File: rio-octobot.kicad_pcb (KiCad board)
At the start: 2 copper layers, 100 x 100 mm, 128 parts, among them J1 Conn_01x06, J10 Conn_01x03, J11 Conn_01x03, J12 Conn_01x03, J13 Conn_01x13, J14 Conn_01x12, J2 Conn_01x06, J3 Conn_01x06, J4 Conn_01x06, J5 Conn_01x06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

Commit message: fixing labels / add some values
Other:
- board text added: "12v GND 5v EN STP DIR"
- board text removed: "12v GND 5v EN DIR STP"
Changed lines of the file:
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@@
     (effects (font (size 1 1) (thickness 0.15)) (justify left bottom))
   )
-  (gr_text "12v GND 5v EN DIR STP" (at 127 74.93 90) (layer "F.SilkS")
+  (gr_text "12v GND 5v EN STP DIR" (at 127 74.93 90) (layer "F.SilkS")
     (effects (font (size 1 1) (thickness 0.15)) (justify left bottom))
   )
@@
     (effects (font (size 1 1) (thickness 0.15)) (justify left bottom))
   )
-  (gr_text "12v GND 5v EN DIR STP" (at 91.44 74.93 90) (layer "F.SilkS")
+  (gr_text "12v GND 5v EN STP DIR" (at 91.44 74.93 90) (layer "F.SilkS")
     (effects (font (size 1 1) (thickness 0.15)) (justify left bottom))
   )
@@
     (effects (font (size 1 1) (thickness 0.15)) (justify left bottom))
   )
-  (gr_text "12v GND 5v EN DIR STP" (at 73.66 74.93 90) (layer "F.SilkS")
+  (gr_text "12v GND 5v EN STP DIR" (at 73.66 74.93 90) (layer "F.SilkS")
     (effects (font (size 1 1) (thickness 0.15)) (justify left bottom))
   )
@@
     (effects (font (size 1 1) (thickness 0.15)) (justify left bottom))
   )
-  (gr_text "12v GND 5v EN DIR STP" (at 82.55 74.93 90) (layer "F.SilkS")
+  (gr_text "12v GND 5v EN STP DIR" (at 82.55 74.93 90) (layer "F.SilkS")
     (effects (font (size 1 1) (thickness 0.15)) (justify left bottom))
   )
@@
     (effects (font (size 1 1) (thickness 0.15)) (justify left bottom))
   )
-  (gr_text "12v GND 5v EN DIR STP" (at 109.22 74.93 90) (layer "F.SilkS")
+  (gr_text "12v GND 5v EN STP DIR" (at 109.22 74.93 90) (layer "F.SilkS")
     (effects (font (size 1 1) (thickness 0.15)) (justify left bottom))
   )
@@
     (effects (font (size 2 2) (thickness 0.15)) (justify left bottom))
   )
-  (gr_text "12v GND 5v EN DIR STP" (at 118.11 74.93 90) (layer "F.SilkS")
+  (gr_text "12v GND 5v EN STP DIR" (at 118.11 74.93 90) (layer "F.SilkS")
     (effects (font (size 1 1) (thickness 0.15)) (justify left bottom))
   )
@@
     (effects (font (size 1 1) (thickness 0.15)) (justify left bottom))
   )
-  (gr_text "12v GND 5v EN DIR STP" (at 100.33 74.93 90) (layer "F.SilkS")
+  (gr_text "12v GND 5v EN STP DIR" (at 100.33 74.93 90) (layer "F.SilkS")
     (effects (font (size 1 1) (thickness 0.15)) (justify left bottom))
   )

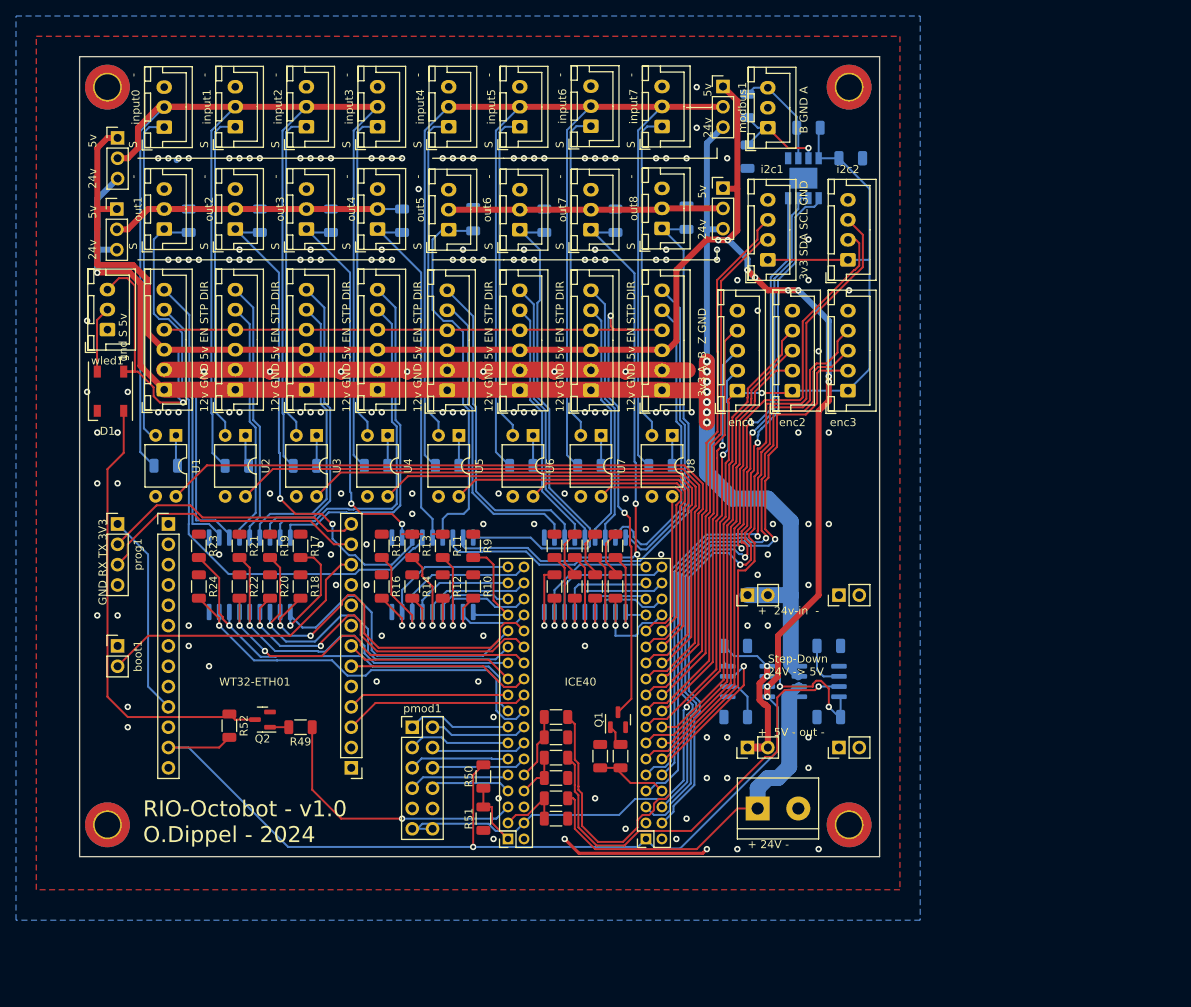
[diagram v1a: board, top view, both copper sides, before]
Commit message: removing level shifter from wled
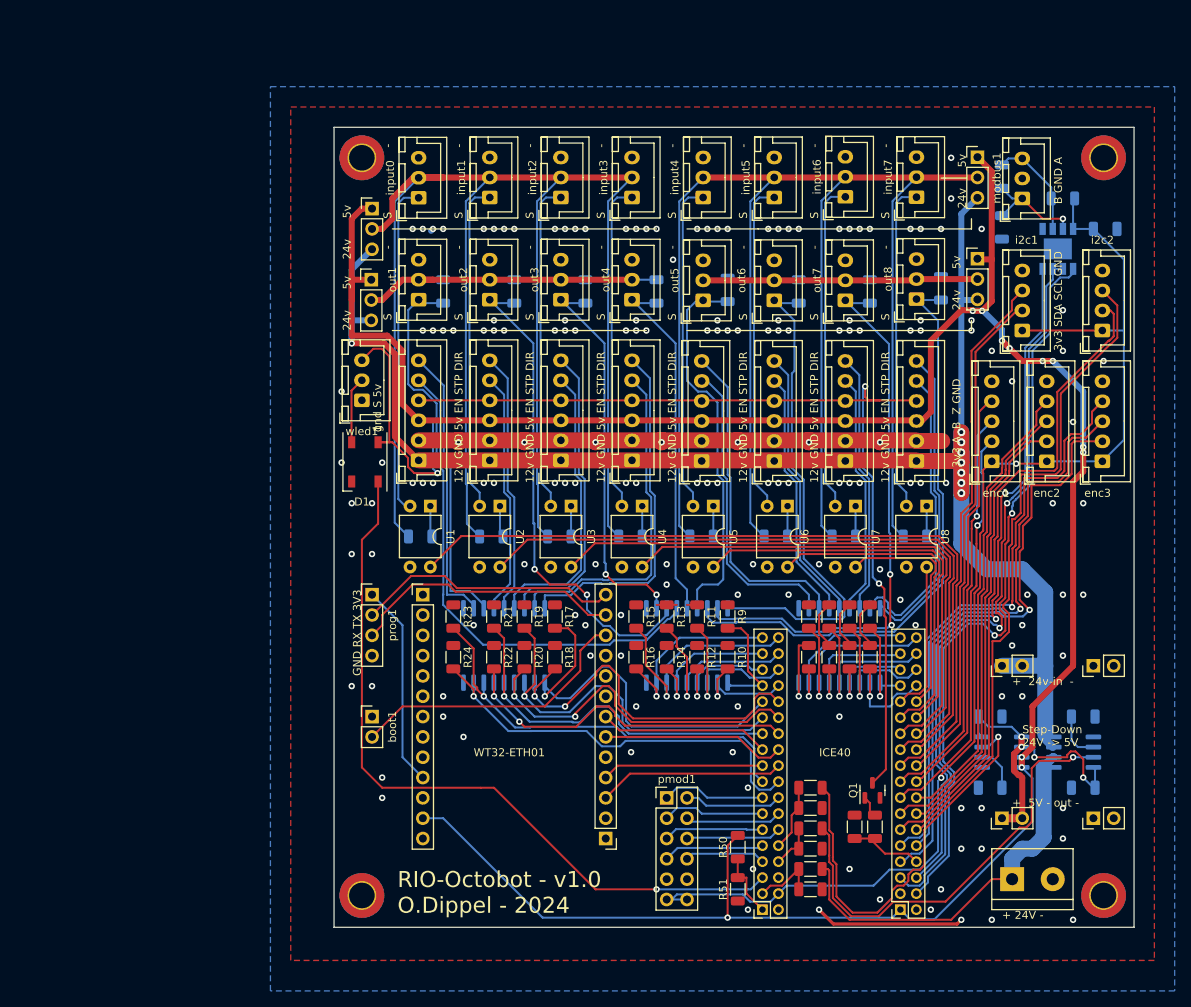
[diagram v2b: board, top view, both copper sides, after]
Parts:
- removed Q2: BC817, Package_TO_SOT_SMD:SOT-23
- removed R49, R52: R, Resistor_SMD:R_1206_3216Metric
- C1, C4: value C -> 1n
- C2, C3, C5: value C -> 100n
- R1, R2, R3, R33, R34, R35, R36, R37, R38, R39, R4, R40, R5, R6, R7, R8: value R -> 3k3
- R10, R11, R12, R13, R14, R15, R16, R17, R18, R19, R20, R21, R22, R23, R24, R55, R9: value R -> 10k
- R41, R47, R48, R50, R51, R53, R54: value R -> 20k
- R42, R43: value R -> 1k
- moved C1 33.0 mm to (182.9, 113.0)
- moved C2 33.0 mm to (182.9, 121.9)
- moved C3 33.0 mm to (185.7, 52.0)
- moved C4 33.0 mm to (171.3, 121.9)
- moved C5 33.0 mm to (171.3, 113.0)
- moved H2 33.0 mm to (185.5, 135.3)
- moved H3 33.0 mm to (185.5, 43.1)
- moved J10 33.0 mm to (169.7, 43.0)
- moved J12 33.0 mm to (169.7, 55.7)
- moved J13 33.0 mm to (100.4, 97.7)
- moved J14 33.0 mm to (123.2, 128.2)
- moved J2 33.0 mm to (108.8, 80.9)
- moved J3 33.0 mm to (117.6, 80.9)
- moved J4 33.0 mm to (126.5, 80.9)
- moved J5 33.0 mm to (135.2, 81.0)
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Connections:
- D1 pad 4: Net-(D1-DIN) -> m7
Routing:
- net m7: track 34.4 -> 93.6 mm
- net Net-(D1-DIN): track 56.5 -> 0.00 mm
- net 5v: track 364.9 -> 356.7 mm
- net Net-(Q2-B): track 2.35 -> 0.00 mm

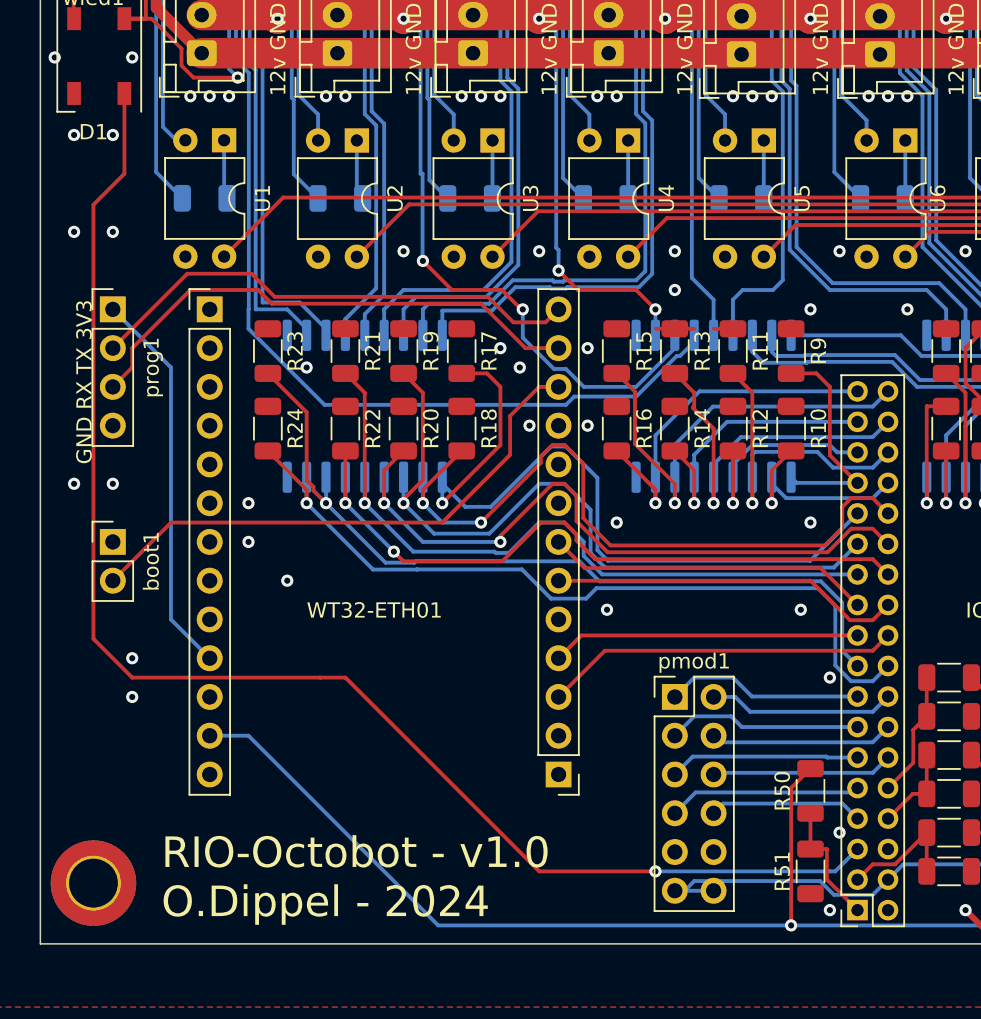
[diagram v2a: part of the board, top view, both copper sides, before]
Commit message: chaning network interface to W5500
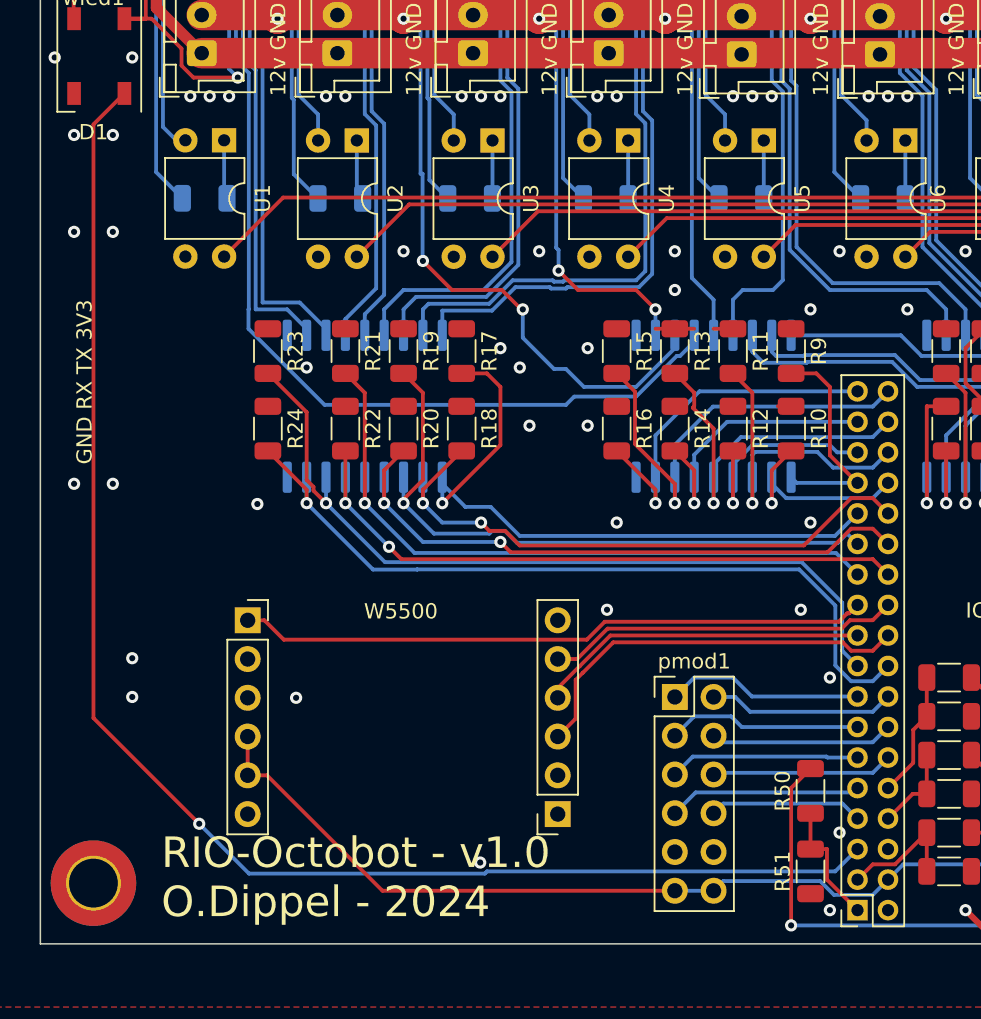
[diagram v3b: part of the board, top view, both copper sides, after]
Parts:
- removed J13: Conn_01x13, Connector_PinHeader_2.54mm:PinHeader_1x13_P2.54mm_Vertical
- removed J14: Conn_01x12, Connector_PinHeader_2.54mm:PinHeader_1x13_P2.54mm_Vertical
- removed boot1: Conn_01x02, Connector_PinHeader_2.54mm:PinHeader_1x02_P2.54mm_Vertical
- removed prog1: Conn_01x04, Connector_PinHeader_2.54mm:PinHeader_1x04_P2.54mm_Vertical
- added J15: Conn_01x06, Connector_PinSocket_2.54mm:PinSocket_1x06_P2.54mm_Vertical, F.Cu at (102.9, 118.1)
- added J16: Conn_01x06, Connector_PinSocket_2.54mm:PinSocket_1x06_P2.54mm_Vertical, F.Cu at (123.2, 130.8)
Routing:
- net 5v: track 356.7 -> 313.5 mm
- net Net-(J14-Pin_11): track 36.0 -> 0.00 mm
- net Net-(J14-Pin_12): track 34.2 -> 0.00 mm
- net Net-(J14-Pin_13): track 32.9 -> 0.00 mm
- net 3v3: track 155.6 -> 187.4 mm
- net Net-(J13-Pin_10): track 25.5 -> 0.00 mm
- net h1: track 21.3 -> 41.4 mm
- net c1: track 50.9 -> 43.5 mm
- net d3: track 46.8 -> 39.5 mm
- net e1: track 47.8 -> 42.8 mm
- net d1: track 45.4 -> 41.1 mm
- net m7: track 93.6 -> 96.7 mm
- net h3: track 23.3 -> 26.3 mm
- net f3: track 45.0 -> 42.6 mm
- net g1: track 47.2 -> 45.0 mm
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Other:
- board text added: "W5500"
- board text removed: "WT32-ETH01"
